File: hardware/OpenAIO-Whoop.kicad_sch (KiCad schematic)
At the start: 0 parts

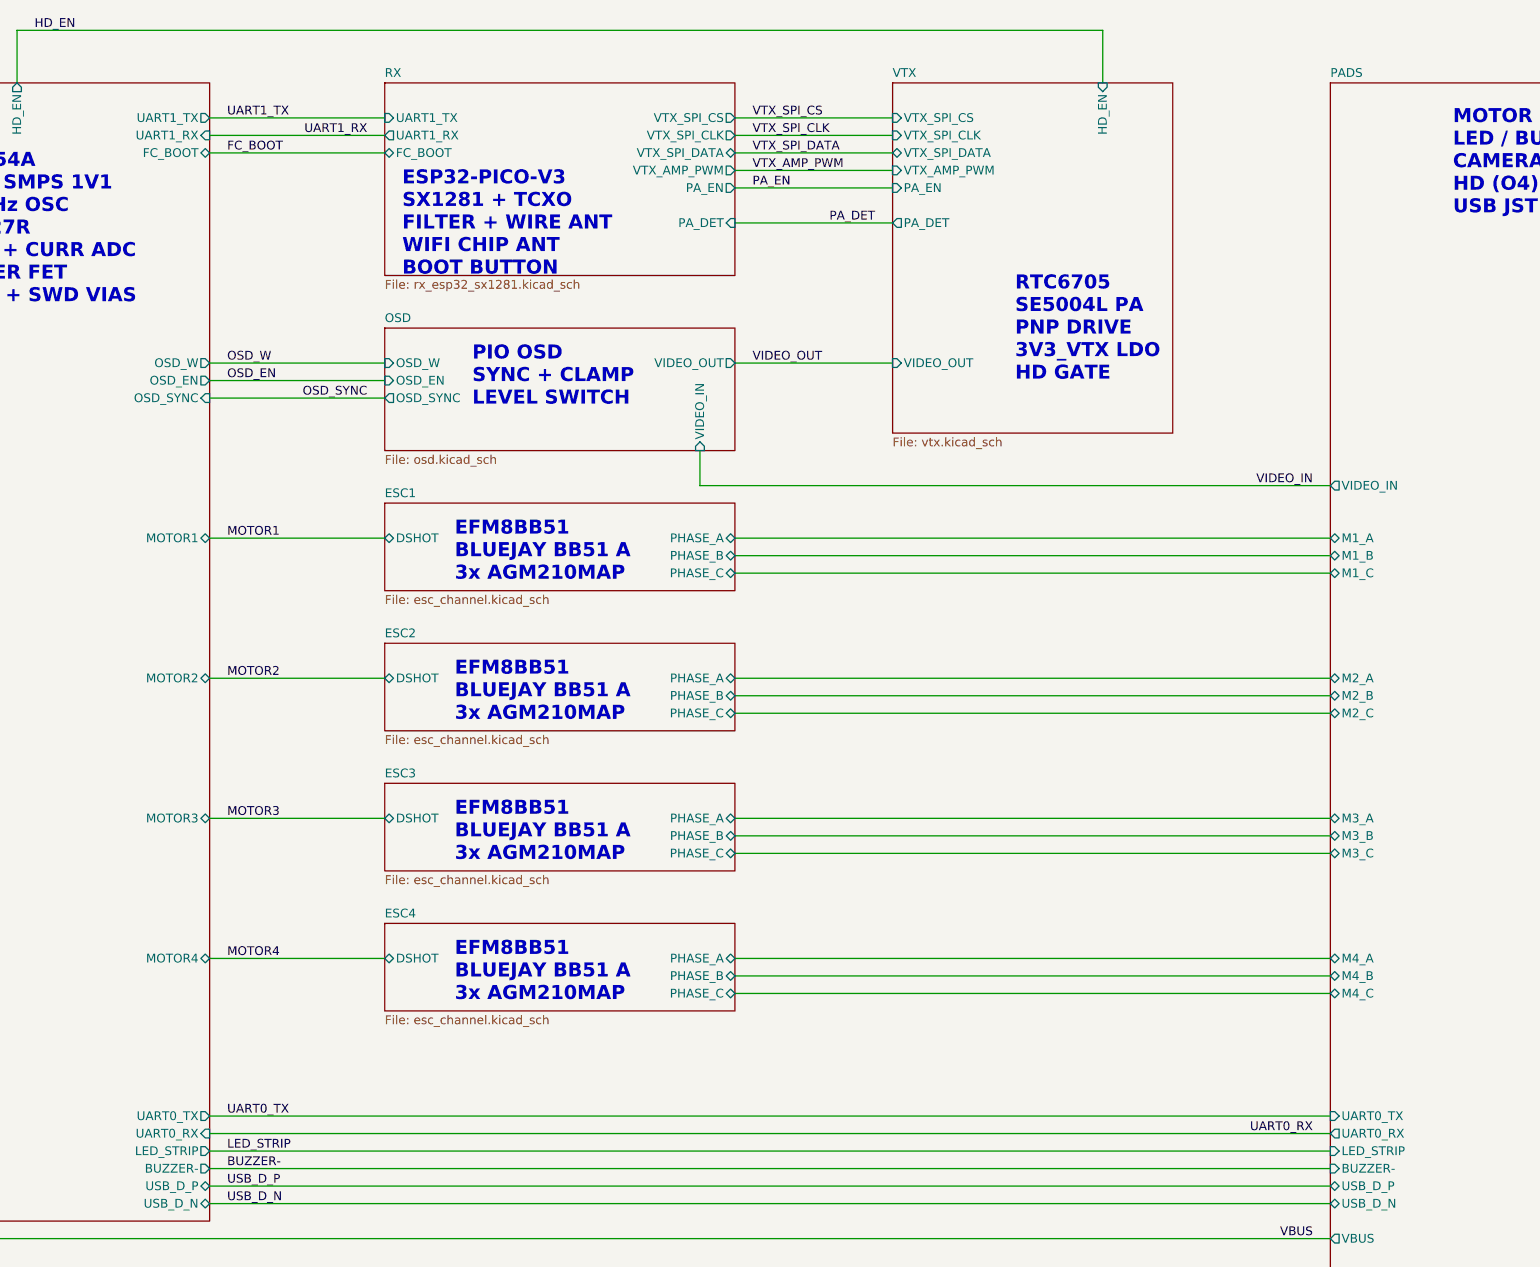
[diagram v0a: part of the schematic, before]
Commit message: Place receiver on south UART and HD on east UART
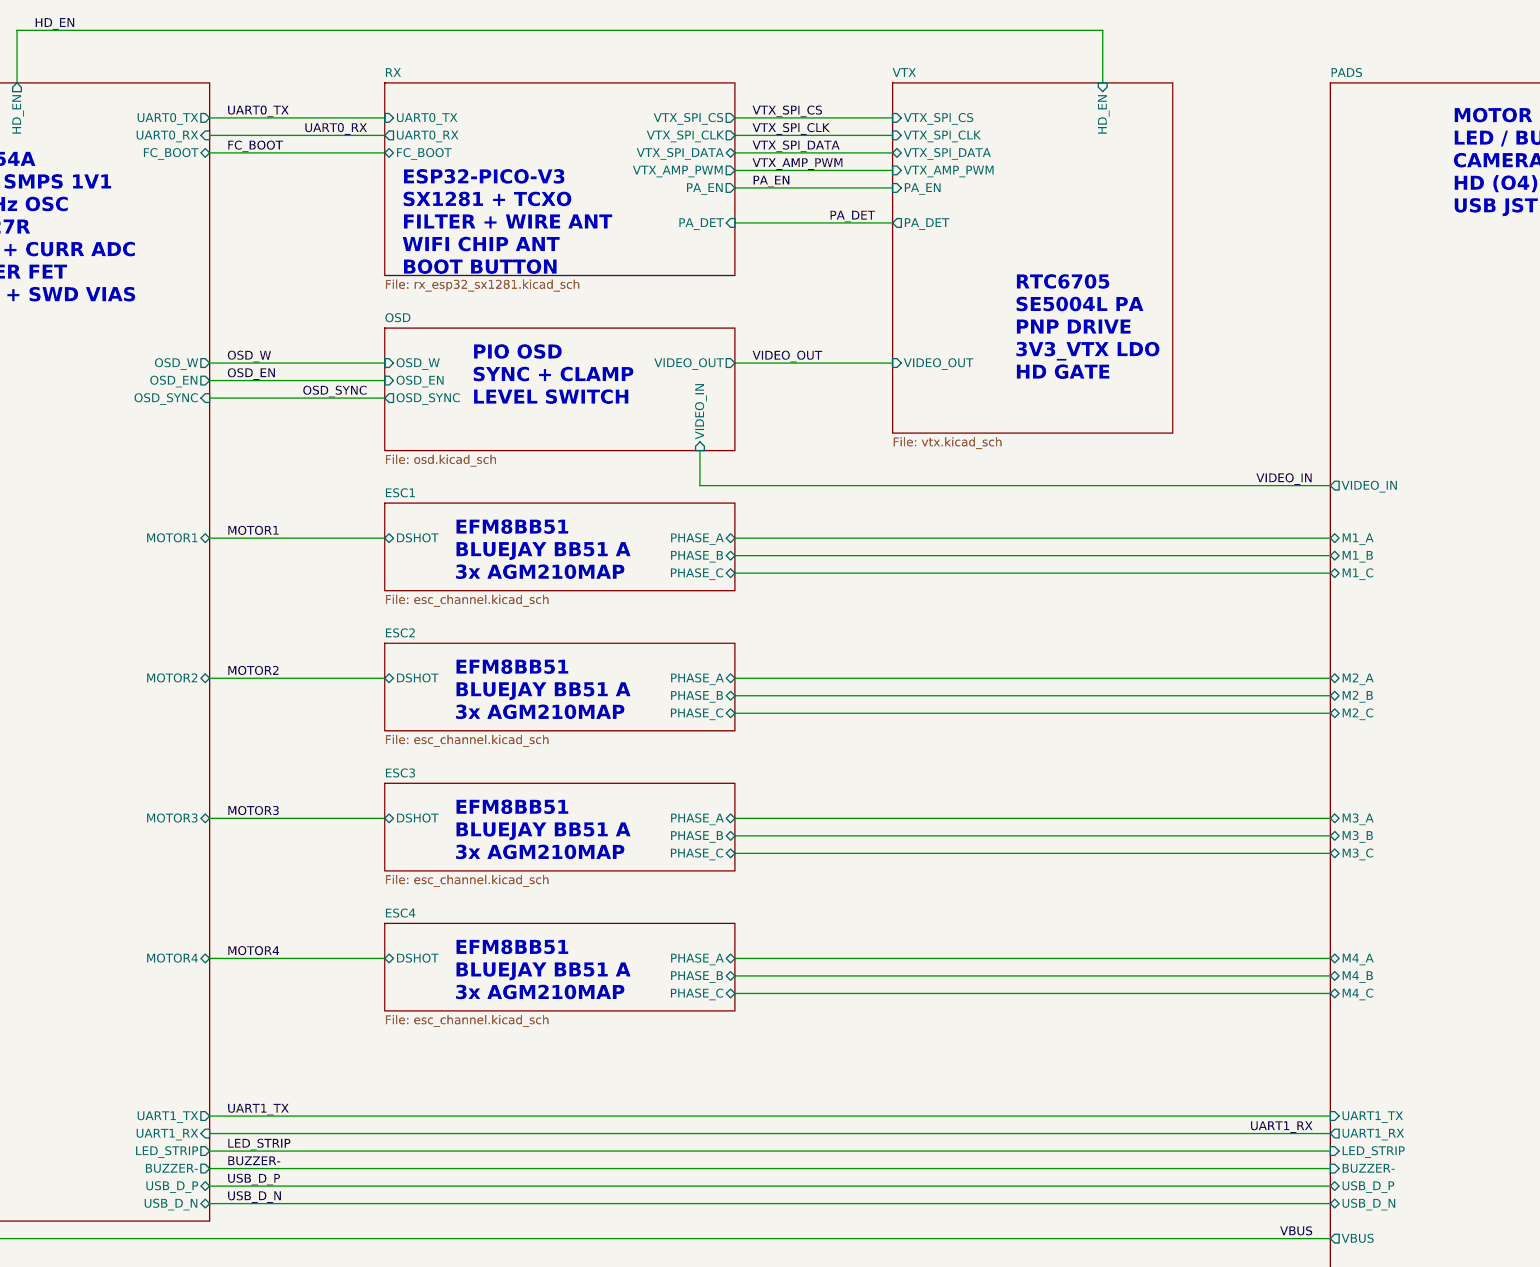
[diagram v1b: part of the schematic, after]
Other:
- sheet PADS ports: added UART1_RX, UART1_TX; removed UART0_RX, UART0_TX
- sheet RX ports: added UART0_RX, UART0_TX; removed UART1_RX, UART1_TX
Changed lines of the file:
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@@
 		)
 	)
-	(label "UART1_TX"
+	(label "UART0_TX"
 		(at 200.66 35.56 0)
 		(effects
@@
 		)
 	)
-	(label "UART0_RX"
+	(label "UART1_RX"
 		(at 358.14 182.88 180)
 		(effects
@@
 		)
 	)
-	(label "UART0_TX"
+	(label "UART1_TX"
 		(at 200.66 180.34 0)
 		(effects
@@
 		)
 	)
-	(label "UART1_RX"
+	(label "UART0_RX"
 		(at 220.98 38.1 180)
 		(effects
@@
 			)
 		)
-		(pin "UART1_TX" input
+		(pin "UART0_TX" input
 			(at 223.52 35.56 180)
 			(effects
@@
 			)
 		)
-		(pin "UART1_RX" output
+		(pin "UART0_RX" output
 			(at 223.52 38.1 180)
 			(effects
@@
 			)
 		)
-		(pin "UART0_TX" input
+		(pin "UART1_TX" input
 			(at 360.68 180.34 180)
 			(effects
@@
 			)
 		)
-		(pin "UART0_RX" output
+		(pin "UART1_RX" output
 			(at 360.68 182.88 180)
 			(effects
@@
 			)
 		)
-		(pin "UART1_TX" output
+		(pin "UART0_TX" output
 			(at 198.12 35.56 0)
 			(effects
@@
 			)
 		)
-		(pin "UART1_RX" input
+		(pin "UART0_RX" input
 			(at 198.12 38.1 0)
 			(effects
@@
 			)
 		)
-		(pin "UART0_TX" output
+		(pin "UART1_TX" output
 			(at 198.12 180.34 0)
 			(effects
@@
 			)
 		)
-		(pin "UART0_RX" input
+		(pin "UART1_RX" input
 			(at 198.12 182.88 0)
 			(effects
@@
 		)
 	)
-	(embedded_fonts no)
 )
